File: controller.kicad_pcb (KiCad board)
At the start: 2 copper layers, 55 x 42 mm, 57 parts, among them J1 Jumper_3_Bridged12, J2 EEPROM DISABLE, J3 Conn_02x20_Odd_Even, J4 5V, J5 USB_B_Mini, J6 Conn_01x05, J7 Jumper_3_Bridged12, SW2 RST, U1 CY7C68013A-56PVX, U2 AZ1117-3.3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

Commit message: let's call this "version 2"
- this is a cleaned-up version of the board that was built and installed in the programmer
- the WAKEUP drain resistor & timing capacitor are included
- the board is hard-wired into the self-powered configuration (USB VBUS only used for WAKEUP)
- power delivery to the FX2 chip is (probably) improved
- the ground plane has fewer interruptions
- (almost) all spare pads and through-holes to accommodate possible mistakes are removed because they're known to not be needed
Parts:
- removed ? (x14): , 
- removed J1, J7: Jumper_3_Bridged12, Jumper:SolderJumper-3_P2.0mm_Open_TrianglePad1.0x1.5mm
- removed R11, R12: 10kΩ, Resistor_SMD:R_0805_2012Metric_Pad1.20x1.40mm_HandSolder
- removed SPARE: SOIC-16_3.9x9.9mm_P1.27mm, Package_SO:SOIC-16_3.9x9.9mm_P1.27mm
- added TP3: PSEN, TestPoint:TestPoint_THTPad_D2.0mm_Drill1.0mm, F.Cu at (169.6, 101.6)
- moved C10 31.1 mm to (130.8, 83.8), turned to 180 degrees
- moved R13 7.31 mm to (130.8, 80.7)
- moved R3 5.09 mm to (135.9, 83.8)
- moved L7 2.70 mm to (128.6, 77.6), turned to 180 degrees
- moved R4 1.55 mm to (135.8, 80.7), turned to 180 degrees
- moved C1 0.06 mm to (157.5, 96.0)
- turned R7 to 0 degrees
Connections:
- D1 pad 1: Net-(D1-K) -> /ACT
- J5 pad 1: Net-(J1-A) -> Net-(J5-VBUS)
- J6 pad 1: Net-(J1-A) -> Net-(J5-VBUS)
- R4 pad 1: Net-(J1-C) -> Net-(J5-VBUS)
- U1 pad 56: Net-(J7-C) -> /ACT
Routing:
- net VCC: track 126.2 -> 82.4 mm, vias 6 -> 5
- net /ACT: track 0.00 -> 39.8 mm
- net Net-(J7-C): track 36.0 -> 0.00 mm, vias 1 -> 0
- net Net-(J5-VBUS): track 0.00 -> 16.3 mm
- net /PSEN: track 24.2 -> 8.24 mm
- net Net-(J1-A): track 11.8 -> 0.00 mm
- net Net-(D1-K): track 10.6 -> 0.00 mm
- net /~{RD}: track 22.4 -> 31.6 mm
- net Net-(U1-WAKEUP): track 41.2 -> 32.7 mm
- net /~{WR}: track 24.5 -> 29.9 mm
- net Net-(J1-C): track 4.10 -> 0.00 mm
- net Net-(U1-~{RESET}): track 48.0 -> 51.9 mm
- net /~{RESET}: track 29.2 -> 30.0 mm
- net GNDREF: track 106.3 -> 105.9 mm, vias 18 -> 17
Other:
- board text added: "ALLPRO88 USB Interface Kipp Cannon 2023"
- board text added: "D+"
- board text added: "D-"
- board text removed: "SELF POWERED: WKUP SEL=VBUS, EXT +5V IN VIA J4 USB POWERED: WKUP SEL=VCC, JUMPER VBUS TO J4"
- board text removed: "WKUP SEL L=VBUS R=VCC"

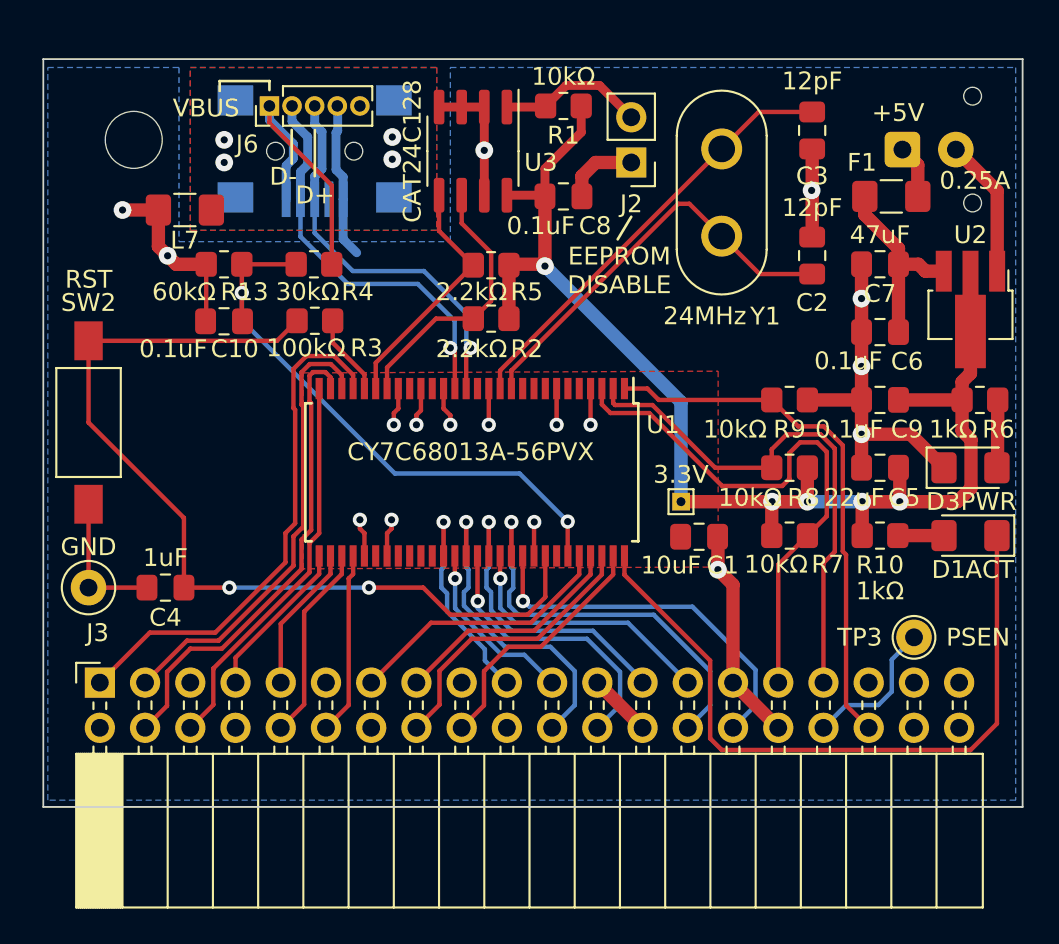
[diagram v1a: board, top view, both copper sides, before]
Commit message: minor improvements
- update to current symbols and footprints
- flip the GPIO and I2C pin headers to the back to avoid damage when the case is opened.  this just changes the silk screen, one can choose to solder them in either way regardless.
- kicad now offers a better crystal footprint.  switch to it so the holes are more appropriately sized
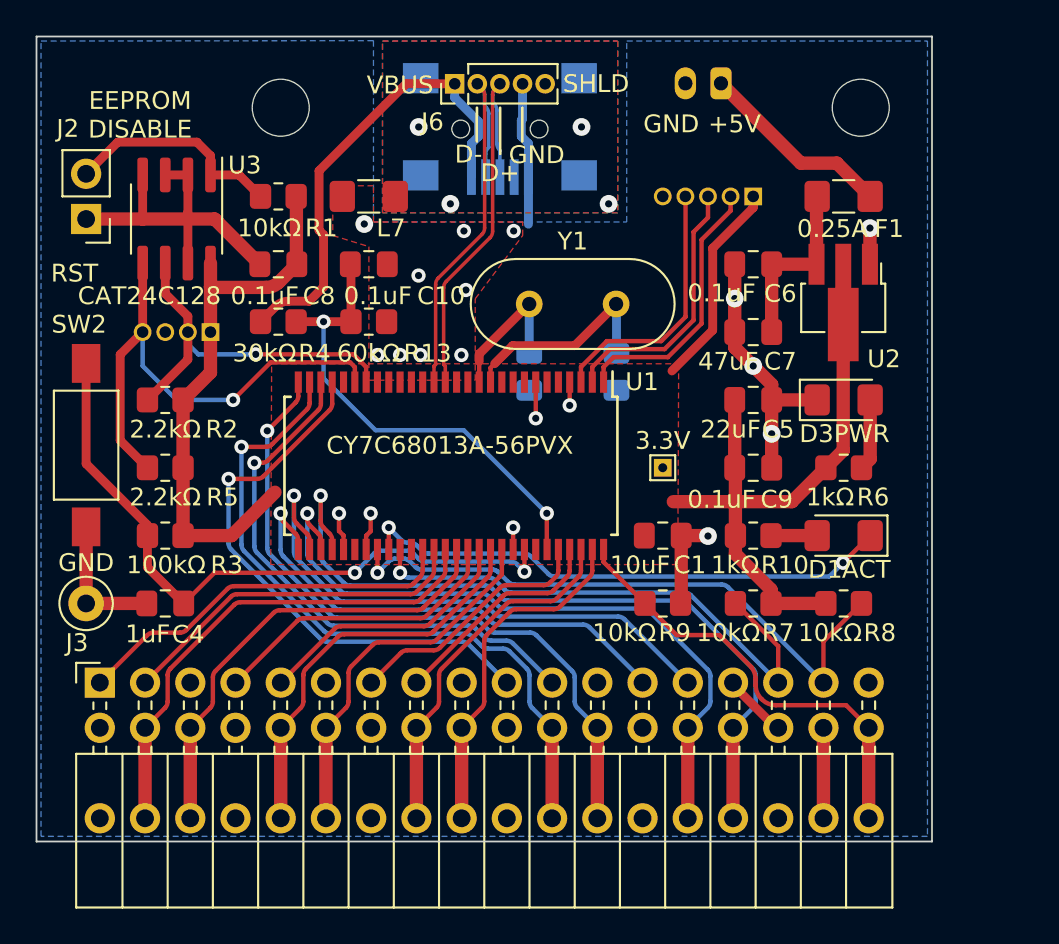
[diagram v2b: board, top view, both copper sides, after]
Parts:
- removed TP3: PSEN, TestPoint:TestPoint_THTPad_D2.0mm_Drill1.0mm
- added H2: MountingHole, MountingHole:MountingHole_3.2mm_M3, F.Cu at (166.6, 71.9)
- added J1: I2C, Connector_PinHeader_1.27mm:PinHeader_1x04_P1.27mm_Vertical, B.Cu at (130.0, 84.5)
- added J7: Conn_01x18, Connector_PinSocket_2.54mm:PinSocket_1x18_P2.54mm_Vertical, F.Cu at (123.8, 111.8)
- added J8: GPIO, Connector_PinHeader_1.27mm:PinHeader_1x05_P1.27mm_Vertical, B.Cu at (160.5, 76.8)
- C2, C3: moved to B.Cu
- J3: value Conn_02x20_Odd_Even -> Conn_02x18_Odd_Even; footprint Connector_PinSocket_2.54mm:PinSocket_2x20_P2.54mm_Horizontal -> Connector_PinSocket_2.54mm:PinSocket_2x18_P2.54mm_Horizontal
- J4: footprint Connector_Molex:Molex_Micro-Fit_3.0_43045-0212_2x01_P3.00mm_Vertical -> Connector_TE-Connectivity:TE_440054-2_1x02_P2.00mm_Vertical
- Y1: footprint Crystal:Crystal_HC50_Vertical -> Crystal:Crystal_HC49-4H_Vertical
- moved J2 30.8 mm to (123.1, 78.1)
- moved R5 21.5 mm to (127.5, 92.1)
- moved C3 20.9 mm to (147.9, 86.7)
- moved R2 18.9 mm to (127.5, 88.3)
- moved U3 17.1 mm to (128.1, 78.1)
- moved R1 16.8 mm to (133.8, 76.8)
- moved C8 16.5 mm to (133.8, 80.6), turned to 180 degrees
- moved R3 14.7 mm to (127.5, 95.9)
- moved Y1 13.9 mm to (147.9, 82.9), turned to 0 degrees
- moved R9 13.5 mm to (155.4, 99.7)
- moved C2 12.8 mm to (152.8, 86.7), turned to 90 degrees
- moved J4 10.8 mm to (158.7, 70.5), turned to 180 degrees
- moved J5 10.5 mm to (146.3, 73.1)
- moved J6 10.5 mm to (143.8, 70.5)
- moved L7 10.4 mm to (138.9, 76.8)
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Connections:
- D1 pad 1: /ACT -> /~{ACT}
- U1 pad 1: /~{RESET} -> /PD5
- U1 pad 2: /~{WR} -> /PD6
- U1 pad 25: /A0 -> /D0
- U1 pad 26: /A1 -> /D1
- U1 pad 27: /A2 -> /D2
- U1 pad 28: /A3 -> /D3
- U1 pad 29: /A4 -> /D4
- U1 pad 3: /~{RD} -> /PD7
- U1 pad 30: /A5 -> /D5
- U1 pad 31: /A6 -> /D6
- U1 pad 32: /A7 -> /D7
- U1 pad 36: unconnected-(U1-CTL0/FLAGA-Pad36) -> /~{WR}
- U1 pad 37: unconnected-(U1-CTL1/FLAGB-Pad37) -> /~{ACT}
- U1 pad 38: unconnected-(U1-CTL2/FLAGC-Pad38) -> /~{RD}
- U1 pad 40: /D0 -> /A0
- U1 pad 41: /D1 -> /A1
- U1 pad 42: /D2 -> /A2
- U1 pad 43: /D3 -> /A3
- U1 pad 44: /D4 -> /A4
- U1 pad 45: /D5 -> /A5
- U1 pad 46: /D6 -> /A6
- U1 pad 47: /D7 -> /A7
- U1 pad 56: /ACT -> /~{RESET}
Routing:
- net /ACT: track 39.8 -> 0.00 mm
- net GNDREF: track 105.9 -> 70.5 mm, vias 17 -> 19
- net /~{ACT}: track 0.00 -> 30.4 mm, vias 0 -> 2
- net /D3: track 16.1 -> 38.8 mm
- net /D7: track 20.9 -> 42.5 mm
- net /D2: track 18.2 -> 39.4 mm
- net /D1: track 10.1 -> 31.0 mm
- net /D0: track 12.5 -> 31.4 mm
- net /D5: track 15.2 -> 31.7 mm
- net Net-(U1-XTALIN): track 24.6 -> 8.32 mm
- net /D6: track 23.2 -> 38.6 mm
- net /PD5: track 0.00 -> 15.2 mm
- net /SDA: track 13.9 -> 29.1 mm, vias 0 -> 1
- net /PD6: track 0.00 -> 14.9 mm
- net /PD7: track 0.00 -> 14.7 mm
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- added copper zone on F.Cu, net GNDREF
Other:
- board size 55 x 42 mm -> 50.3 x 45.2 mm
- board text added: "3.3V"
- board text added: "GND"
- board text added: "PD5"
- board text added: "PD6"
- board text added: "PD7"
- board text added: "SCL"
- board text added: "SDA"
- board text added: "SHLD"
